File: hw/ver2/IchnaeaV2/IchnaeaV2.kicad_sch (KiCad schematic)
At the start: 7 parts, among them J1 Screw_Terminal_01x09, J2 Screw_Terminal_01x09, J3 Screw_Terminal_01x09

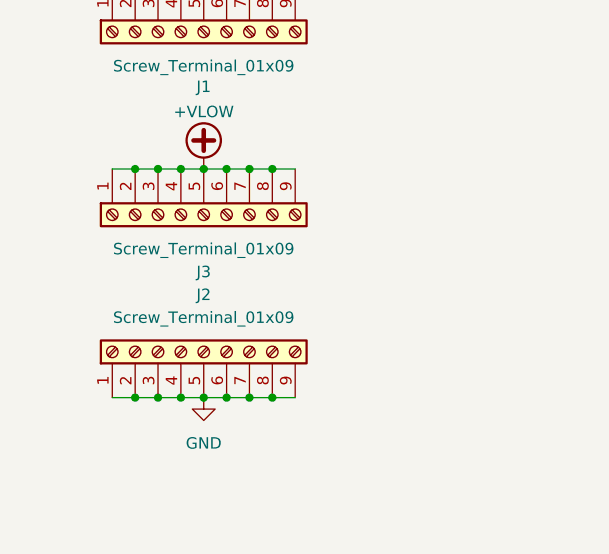
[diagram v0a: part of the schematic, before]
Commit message: Trying to optimize the high power loop area
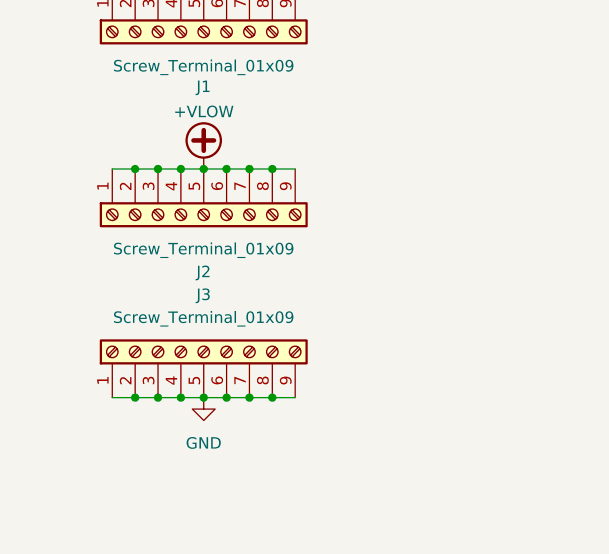
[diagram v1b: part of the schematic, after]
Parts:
- renumbered J3 to J2, J2 to J3
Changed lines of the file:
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@@
 		(on_board yes)
 		(dnp no)
-		(property "Reference" "#PWR08"
+		(property "Reference" "#PWR04"
 			(at 33.02 74.93 0)
 			(effects
@@
 			(project "IchnaeaV2"
 				(path "/93408532-1ffa-463d-873c-16289d2b7987"
-					(reference "#PWR08")
+					(reference "#PWR04")
 					(unit 1)
 				)
@@
 		(on_board yes)
 		(dnp no)
-		(property "Reference" "#PWR07"
+		(property "Reference" "#PWR03"
 			(at 33.02 54.61 0)
 			(effects
@@
 			(project "IchnaeaV2"
 				(path "/93408532-1ffa-463d-873c-16289d2b7987"
-					(reference "#PWR07")
+					(reference "#PWR03")
 					(unit 1)
 				)
@@
 		(dnp no)
 		(fields_autoplaced yes)
-		(property "Reference" "#PWR03"
+		(property "Reference" "#PWR06"
 			(at 44.45 35.56 0)
 			(effects
@@
 			(project "IchnaeaV2"
 				(path "/93408532-1ffa-463d-873c-16289d2b7987"
-					(reference "#PWR03")
+					(reference "#PWR06")
 					(unit 1)
 				)
@@
 		(dnp no)
 		(fields_autoplaced yes)
-		(property "Reference" "J3"
+		(property "Reference" "J2"
 			(at 33.02 83.82 90)
 			(effects
@@
 			(project "IchnaeaV2"
 				(path "/93408532-1ffa-463d-873c-16289d2b7987"
-					(reference "J3")
+					(reference "J2")
 					(unit 1)
 				)
@@
 		(dnp no)
 		(fields_autoplaced yes)
-		(property "Reference" "#PWR04"
+		(property "Reference" "#PWR07"
 			(at 44.45 48.26 0)
 			(effects
@@
 			(project "IchnaeaV2"
 				(path "/93408532-1ffa-463d-873c-16289d2b7987"
-					(reference "#PWR04")
+					(reference "#PWR07")
 					(unit 1)
 				)
@@
 		(dnp no)
 		(fields_autoplaced yes)
-		(property "Reference" "J2"
+		(property "Reference" "J3"
 			(at 33.02 86.36 90)
 			(effects
@@
 			(project "IchnaeaV2"
 				(path "/93408532-1ffa-463d-873c-16289d2b7987"
-					(reference "J2")
-					(unit 1)
-				)
+					(reference "J3")
+					(unit 1)
+				)

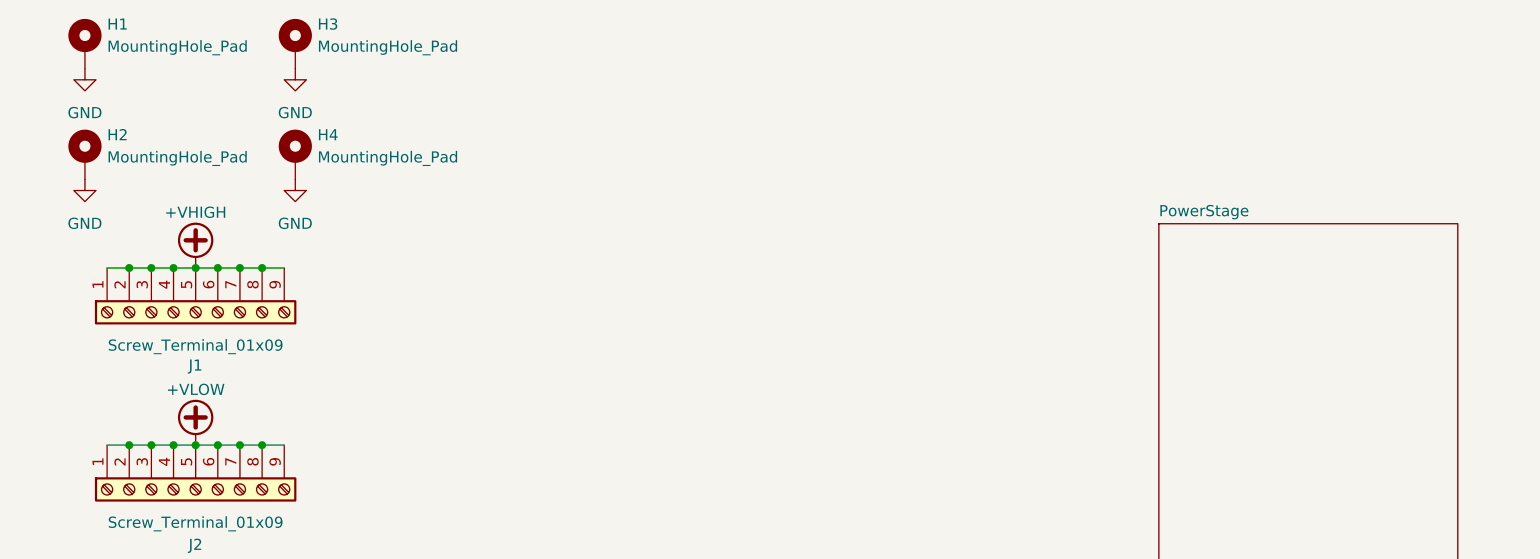
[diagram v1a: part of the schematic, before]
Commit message: Trying to further compress power loop area
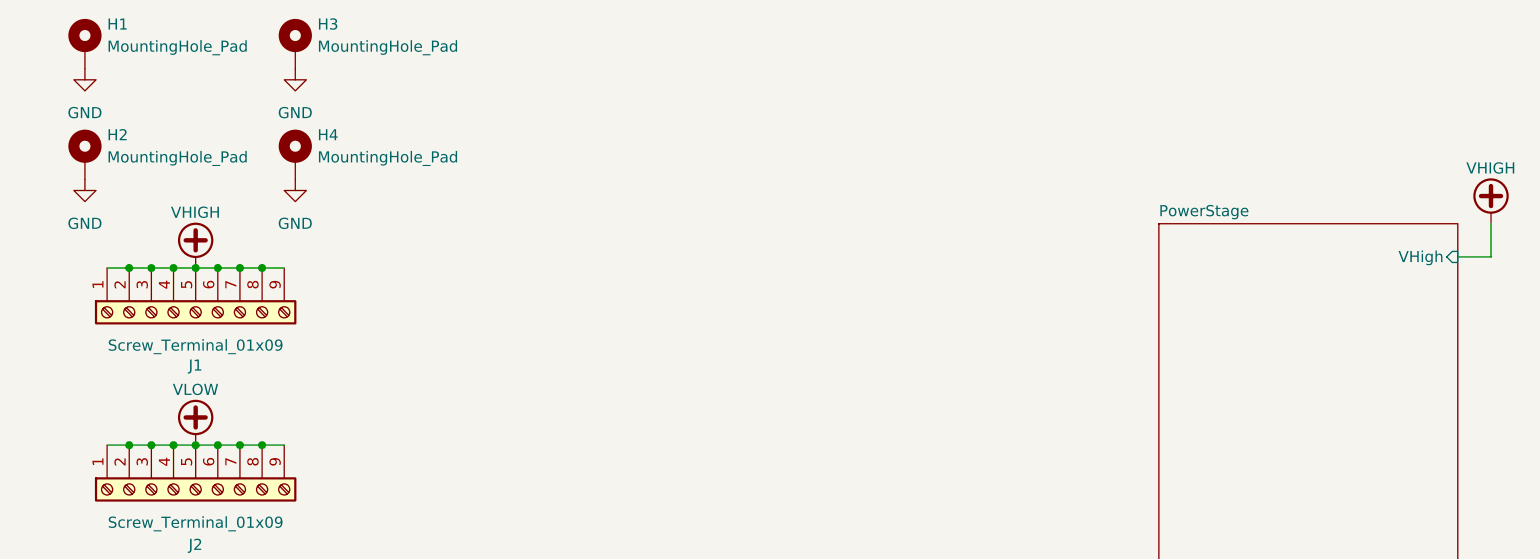
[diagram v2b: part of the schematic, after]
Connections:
- net +VHIGH renamed VHIGH
- net +VLOW renamed VLOW
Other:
- sheet PowerStage ports: added VHigh; removed none
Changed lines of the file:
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@@
+	(wire
+		(pts
+			(xy 177.8 50.8) (xy 181.61 50.8)
+		)
+		(stroke
+			(width 0)
+			(type default)
+		)
+	)
 	(wire
 		(pts
@@
 		(pts
 			(xy 38.1 52.07) (xy 40.64 52.07)
+		)
+		(stroke
+			(width 0)
+			(type default)
+		)
+	)
+	(wire
+		(pts
+			(xy 181.61 50.8) (xy 181.61 46.99)
 		)
 		(stroke
@@
 			)
 		)
-		(property "Value" "+VLOW"
+		(property "Value" "VLOW"
 			(at 33.02 66.04 0)
 			(effects
@@
 			)
 		)
-		(property "Value" "+VHIGH"
+		(property "Value" "VHIGH"
 			(at 33.02 45.72 0)
 			(effects
@@
 				(path "/93408532-1ffa-463d-873c-16289d2b7987"
 					(reference "J2")
+					(unit 1)
+				)
+			)
+		)
+	)
+	(symbol
+		(lib_id "power:+VDC")
+		(at 181.61 46.99 0)
+		(unit 1)
+		(exclude_from_sim no)
+		(in_bom yes)
+		(on_board yes)
+		(dnp no)
+		(property "Reference" "#PWR092"
+			(at 181.61 49.53 0)
+			(effects
+				(font
+					(size 1.27 1.27)
+				)
+				(hide yes)
+			)
+		)
+		(property "Value" "VHIGH"
+			(at 181.61 40.64 0)
+			(effects
+				(font
+					(size 1.27 1.27)
+				)
+			)
+		)
+		(property "Footprint" ""
+			(at 181.61 46.99 0)
+			(effects
+				(font
+					(size 1.27 1.27)
+				)
+				(hide yes)
+			)
+		)
+		(property "Datasheet" ""
+			(at 181.61 46.99 0)
+			(effects
+				(font
+					(size 1.27 1.27)
+				)
+				(hide yes)
+			)
+		)
+		(property "Description" "Power symbol creates a global label with name \"+VDC\""
+			(at 181.61 46.99 0)
+			(effects
+				(font
+					(size 1.27 1.27)
+				)
+				(hide yes)
+			)
+		)
+		(pin "1"
+		)
+		(instances
+			(project "IchnaeaV2"
+				(path "/93408532-1ffa-463d-873c-16289d2b7987"
+					(reference "#PWR092")
 					(unit 1)
 				)
@@
 			)
 		)
+		(pin "VHigh" input
+			(at 177.8 50.8 0)
+			(effects
+				(font
+					(size 1.27 1.27)
+				)
+				(justify right)
+			)
+		)

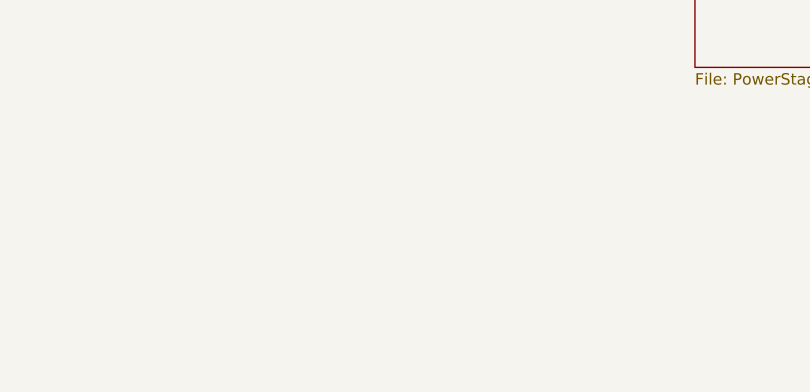
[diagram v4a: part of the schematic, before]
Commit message: More power stage layout
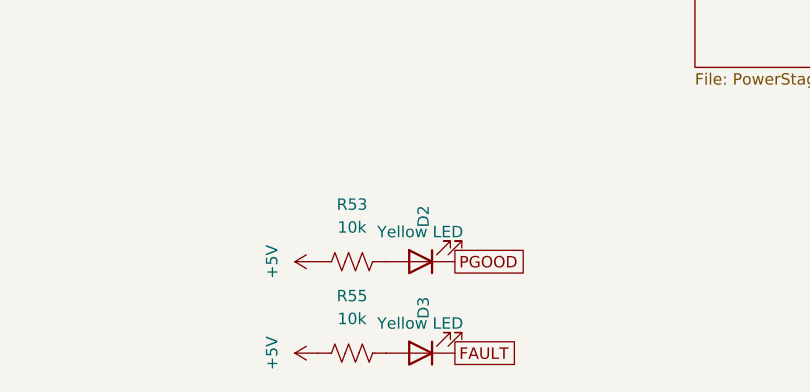
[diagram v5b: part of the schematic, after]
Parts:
- added D2, D3: Yellow LED, LED_SMD:LED_0805_2012Metric, symbol Device:LED
- added R53, R55: 10k, Resistor_SMD:R_0603_1608Metric, symbol Device:R_US
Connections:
- new net: D2.2 (A), R53.1
- new net: D3.2 (A), R55.1
- new net +5V: R53.2, R55.2
- new net FAULT: D3.1 (K)
- new net PGOOD: D2.1 (K)

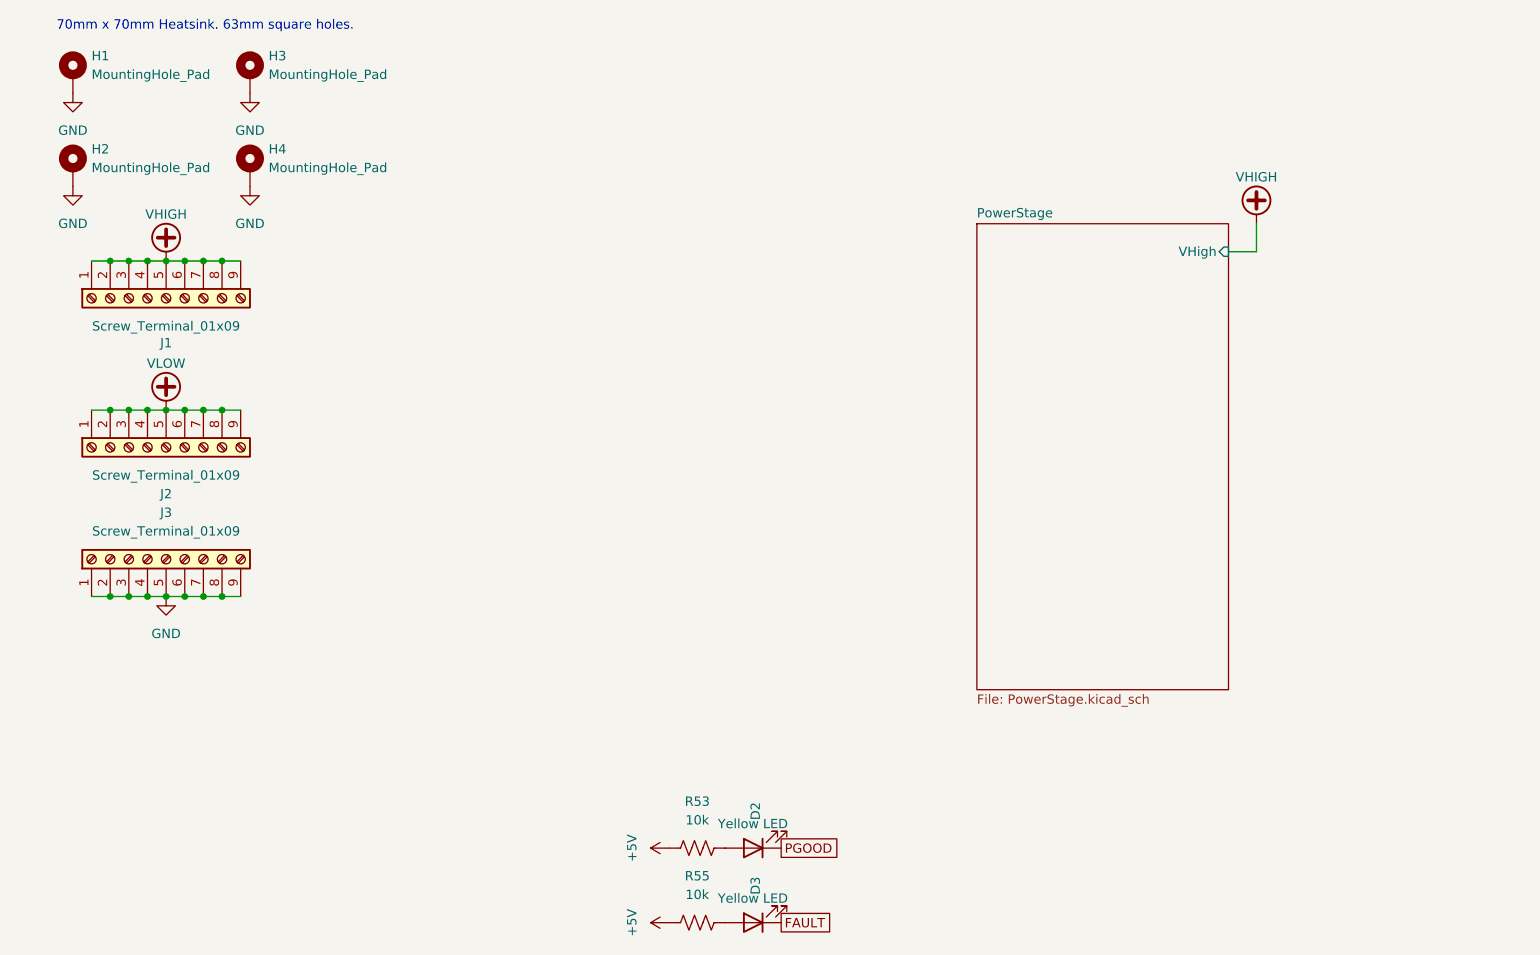
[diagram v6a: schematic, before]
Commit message: Partially work through the V1 notes. Start adding some of the control stage circuitry.
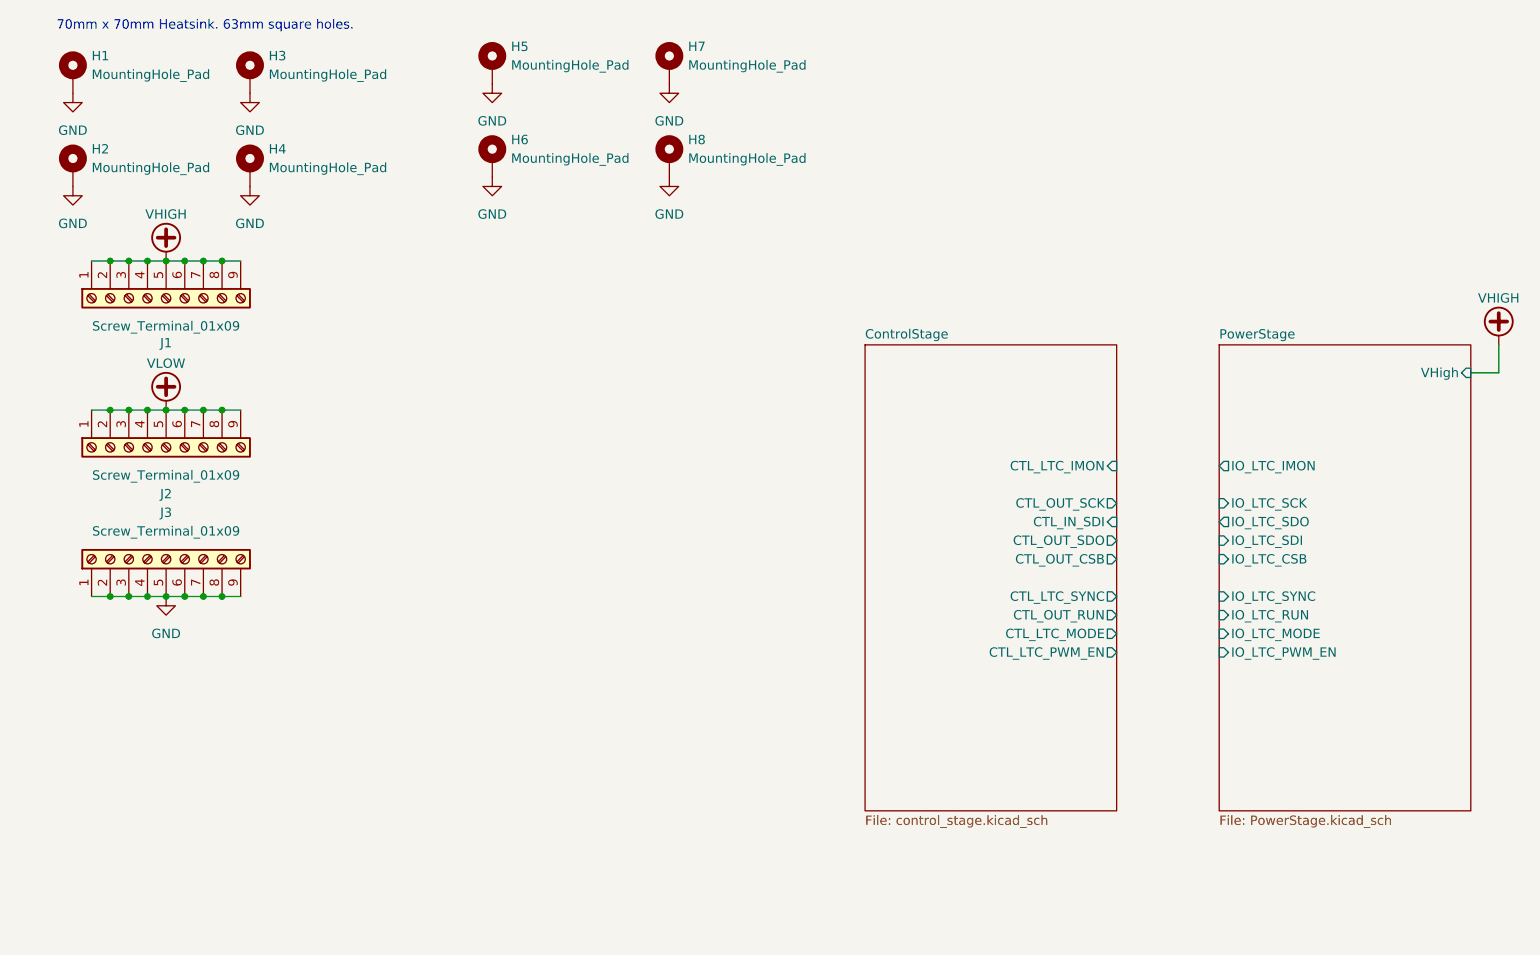
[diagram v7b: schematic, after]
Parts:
- removed D2, D3: Yellow LED, LED_SMD:LED_0805_2012Metric, symbol Device:LED
- removed R53, R55: 10k, Resistor_SMD:R_0603_1608Metric, symbol Device:R_US
- added H5, H6, H7, H8: MountingHole_Pad, MountingHole:MountingHole_3.2mm_M3_Pad_Via, symbol Mechanical:MountingHole_Pad
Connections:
- net GND: now also H5.1, H6.1, H7.1, H8.1
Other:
- added sheet ControlStage (control_stage.kicad_sch)
- sheet PowerStage ports: added IO_LTC_CSB, IO_LTC_IMON, IO_LTC_MODE, IO_LTC_PWM_EN, IO_LTC_RUN, IO_LTC_SCK, IO_LTC_SDI, IO_LTC_SDO, IO_LTC_SYNC; removed none

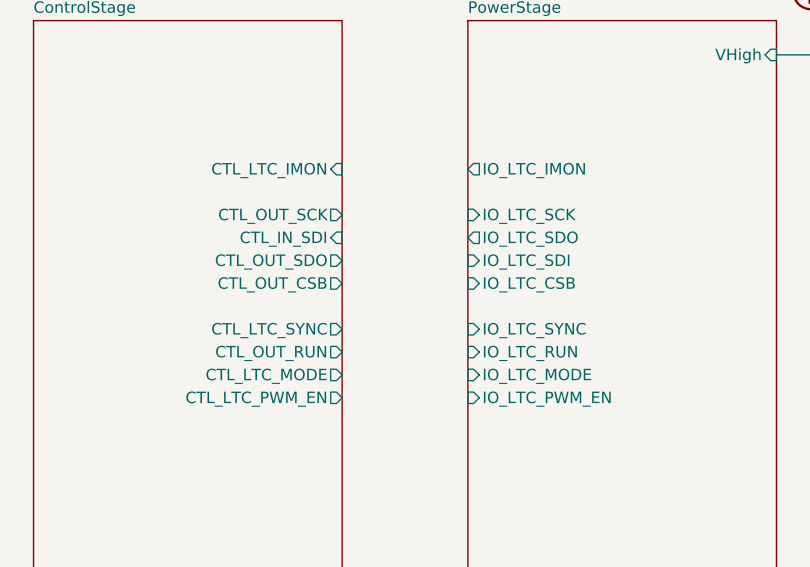
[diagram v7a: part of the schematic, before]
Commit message: Partial pin mapping. ESD protection on signals that exit the board.
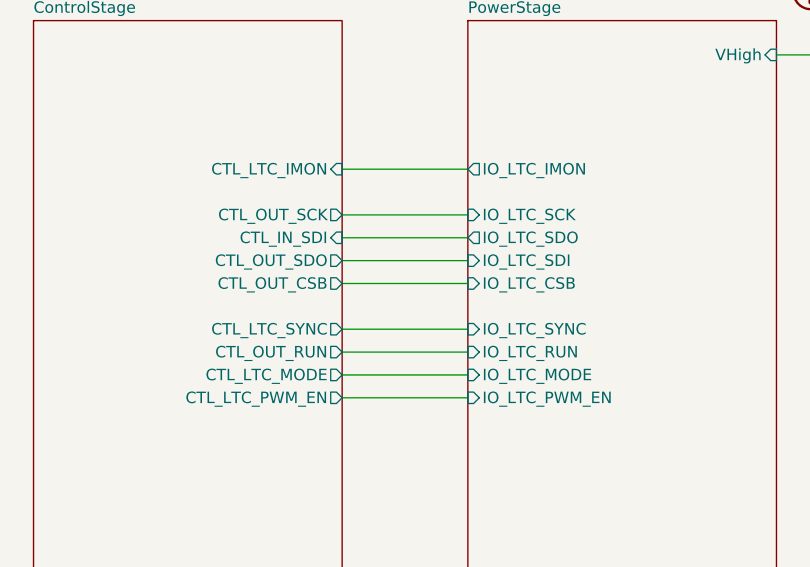
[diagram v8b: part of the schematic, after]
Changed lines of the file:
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@@
+	(wire
+		(pts
+			(xy 162.56 87.63) (xy 176.53 87.63)
+		)
+		(stroke
+			(width 0)
+			(type default)
+		)
+	)
+	(wire
+		(pts
+			(xy 162.56 92.71) (xy 176.53 92.71)
+		)
+		(stroke
+			(width 0)
+			(type default)
+		)
+	)
+	(wire
+		(pts
+			(xy 162.56 90.17) (xy 176.53 90.17)
+		)
+		(stroke
+			(width 0)
+			(type default)
+		)
+	)
+	(wire
+		(pts
+			(xy 162.56 100.33) (xy 176.53 100.33)
+		)
+		(stroke
+			(width 0)
+			(type default)
+		)
+	)
 	(wire
 		(pts
@@
 	(wire
 		(pts
+			(xy 162.56 80.01) (xy 176.53 80.01)
+		)
+		(stroke
+			(width 0)
+			(type default)
+		)
+	)
+	(wire
+		(pts
 			(xy 30.48 52.07) (xy 33.02 52.07)
 		)
@@
 	(wire
 		(pts
+			(xy 162.56 105.41) (xy 176.53 105.41)
+		)
+		(stroke
+			(width 0)
+			(type default)
+		)
+	)
+	(wire
+		(pts
 			(xy 38.1 52.07) (xy 40.64 52.07)
 		)
@@
 	(wire
 		(pts
+			(xy 162.56 102.87) (xy 176.53 102.87)
+		)
+		(stroke
+			(width 0)
+			(type default)
+		)
+	)
+	(wire
+		(pts
 			(xy 30.48 97.79) (xy 33.02 97.79)
 		)
@@
 		)
 		(stroke
+			(width 0)
+			(type default)
+		)
+	)
+	(wire
+		(pts
+			(xy 162.56 85.09) (xy 176.53 85.09)
+		)
+		(stroke
+			(width 0)
+			(type default)
+		)
+	)
+	(wire
+		(pts
+			(xy 162.56 97.79) (xy 176.53 97.79)
+		)
+		(stroke
